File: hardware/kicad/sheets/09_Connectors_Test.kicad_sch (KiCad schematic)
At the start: 0 parts

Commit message: Complete ECO-003 hierarchy exposure
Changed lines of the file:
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@@
+    (effects (font (size 1.27 1.27)) (justify left))
+  )
+  (hierarchical_label "J6_I2C_SDA" (shape bidirectional) (at 100 60.24 0)
+    (effects (font (size 1.27 1.27)) (justify left))
+  )
+  (hierarchical_label "J6_I2C_SCL" (shape input) (at 100 65.32 0)
+    (effects (font (size 1.27 1.27)) (justify left))
+  )
+  (hierarchical_label "J7_I2C_SDA" (shape bidirectional) (at 100 70.40 0)
+    (effects (font (size 1.27 1.27)) (justify left))
+  )
+  (hierarchical_label "J7_I2C_SCL" (shape input) (at 100 75.48 0)
     (effects (font (size 1.27 1.27)) (justify left))
   )

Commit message: Implement Package 10R connector interfaces
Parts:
- added DFT1: T1 factory pogo logical boundary; not populated, symbol IPC100:CONN6
- added J1: P1/H01 controller input, symbol IPC100:CONN2
- added J10: D1/H10 ICD-001 optional DNP; no live mate, symbol IPC100:CONN4
- added J13: U1/H13 USB2 device-UFP grouped contacts, symbol IPC100:CONN12
- added J2: M1/H02 Axis 1 logic, symbol IPC100:CONN6
- added J3: M1/H03 Axis 2 logic, symbol IPC100:CONN6
- added J4: S1/H04 LEFT-RIGHT limits, symbol IPC100:CONN4
- added J5: S1/H05 UP-DOWN limits, symbol IPC100:CONN4
- added J6: D1/H06 OLED; 0.20m; no live mate, symbol IPC100:CONN5
- added J7: D1/H07 BME280; 0.20m; no live mate, symbol IPC100:CONN4
- added J8A: S1/H08A dedicated STOP; unique key, symbol IPC100:CONN2
- added J8B: L1/H08B ordinary UI; incompatible with J8A, symbol IPC100:CONN12
- added J9: R1/H09 SELV dry contact; 0-30VDC 1A, symbol IPC100:CONN3
- added R1: 5.1 kΩ ±1% CC1 Rd, symbol IPC100:R
- added R2: 5.1 kΩ ±1% CC2 Rd, symbol IPC100:R
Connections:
- net +3V3_CORE: now also DFT1.1, J8B.11
- net ARM_IN_RAW: now also J8B.6
- net AXIS1_LEN_SAFE: now also J2.1
- net AXIS1_LPWM_SAFE: now also J2.3
- net AXIS1_REN_SAFE: now also J2.2
- net AXIS1_RPWM_SAFE: now also J2.4
- net AXIS2_LEN_SAFE: now also J3.1
- net AXIS2_LPWM_SAFE: now also J3.3
- net AXIS2_REN_SAFE: now also J3.2
- net AXIS2_RPWM_SAFE: now also J3.4
- net BUZZER_OUT: now also J8B.1
- net ENCODER_A_RAW: now also J8B.9
- net ENCODER_B_RAW: now also J8B.8
- net ENCODER_SW_RAW: now also J8B.7
- net ESP_BOOT: now also DFT1.3
- net ESP_EN: now also DFT1.4
- net EXPANSION_VCC: now also J10.4
- net FIRE_IN_RAW: now also J8B.5
- net J10_I2C_SCL: now also J10.1
- net J10_I2C_SDA: now also J10.2
- net J6_I2C_SCL: now also J6.2
- net J6_I2C_SDA: now also J6.3
- net J7_I2C_SCL: now also J7.1
- net J7_I2C_SDA: now also J7.2
- net LIMIT_DOWN_RAW: now also J5.2
- net LIMIT_DOWN_RETURN: now also J5.1
- net LIMIT_LEFT_RAW: now also J4.4
- net LIMIT_LEFT_RETURN: now also J4.3
- net LIMIT_RIGHT_RAW: now also J4.2
- net LIMIT_RIGHT_RETURN: now also J4.1
- net LIMIT_UP_RAW: now also J5.4
- net LIMIT_UP_RETURN: now also J5.3
- net MOTOR_LOGIC_5V_A: now also J2.6
- net MOTOR_LOGIC_5V_B: now also J3.6
- net OLED_RESET: now also J6.1
- net OLED_VCC: now also J6.5
- net RELAY_COM: now also J9.2
- net RELAY_NC: now also J9.3
- net RELAY_NO: now also J9.1
- net RGB_B: now also J8B.2
- net RGB_G: now also J8B.3
- net RGB_R: now also J8B.4
- net SENSOR_VCC: now also J7.4
- net STOP_IN_RAW: now also J8A.2
- net STOP_RETURN: now also J8A.1
- net UART0_RX: now also DFT1.5
- net UART0_TX: now also DFT1.6
- net UI_VCC: now also J8B.10
- net USB_D+: now also J13.7, J13.8
- net USB_D-: now also J13.5, J13.6
- net USB_VBUS_RAW: now also J13.11, J13.12
- net VIN_RAW: now also J1.2
- new net GND: DFT1.2, J1.1, J10.3, J13.3, J13.4, J2.5, J3.5, J6.4, J7.3, J8B.12, R1.1, R2.1
- new net USB_CC1_RD_5K1: J13.10, R1.2
- new net USB_CC2_RD_5K1: J13.9, R2.2
- new net USB_SHIELD: J13.2
- no-connect marks 0 -> 1
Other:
- note added: "DFT1 FACTORY POGO: UART0_TX, UART0_RX, ESP_EN, ESP_BOOT, GND, +3V3_CORE sense-only; ground first; fixture never sources 3V3."
- note added: "J11 — DOCUMENTATION ONLY: spare GPIO concept; no symbol, pads, harness, or Rev A electrical connectivity. GPIO37 reserved."
- note added: "J12 — DOCUMENTATION ONLY: future CAN/RS485 concept; no symbol, pads, harness, or Rev A electrical connectivity."
- note added: "J13 U1: USB 2.0 DEVICE/UFP ONLY; 5.1k Rd on CC1/CC2 and connector ESD/shield options remain exact-part release items; no PD/host/source."
- note added: "PACKAGE 10R — ICD-002 PHYSICAL CONNECTOR BOUNDARIES; GENERIC SYMBOLS; NO FOOTPRINTS OR FINAL PART NUMBERS"

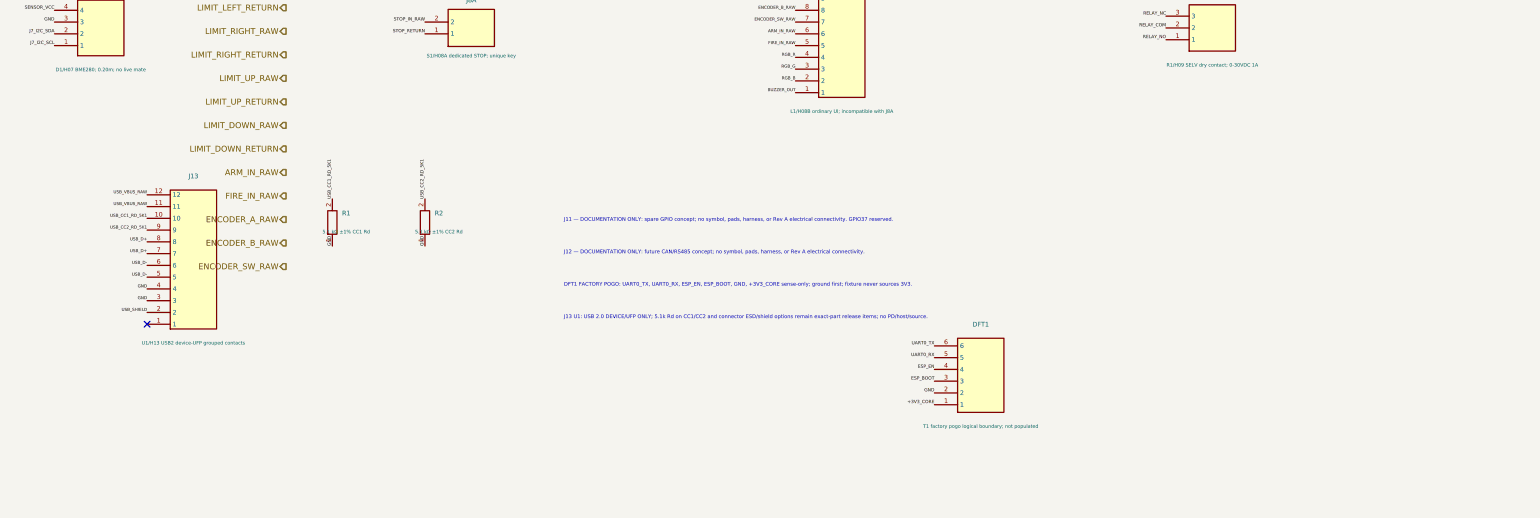
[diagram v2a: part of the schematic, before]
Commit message: Complete ECO-004 interface remediation
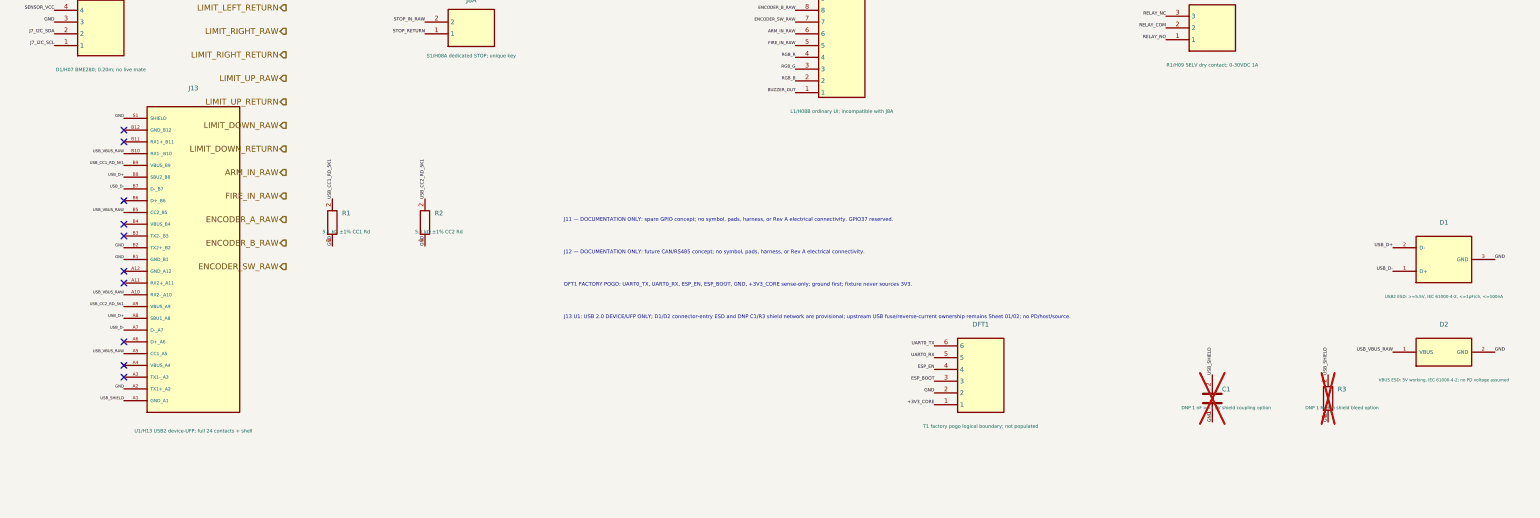
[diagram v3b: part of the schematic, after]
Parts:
- added C1: DNP 1 nF >=1 kV shield coupling option, symbol IPC100:C
- added D1: USB2 ESD: >=5.5V, IEC 61000-4-2, <=1pF/ch, <=100nA, symbol IPC100:USB_ESD2
- added D2: VBUS ESD: 5V working, IEC 61000-4-2; no PD voltag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, symbol IPC100:VBUS_ESD
- added R3: DNP 1 MOhm shield bleed option, symbol IPC100:R
- J13: value U1/H13 USB2 device-UFP grouped contacts -> U1/H13 USB2 device-UFP; full 24 contacts + shell; symbol IPC100:CONN12 -> IPC100:USB_C_UFP_FULL
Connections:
- net GND: now also J13.A2 (TX1+_A2), J13.B1 (GND_B1), J13.B2 (TX2+_B2), J13.S1 (SHIELD), C1.1, D1.3 (GND), D2.2 (GND), R3.1; no longer J13.3, J13.4
- net USB_CC1_RD_5K1: now also J13.B9 (VBUS_B9); no longer J13.10
- net USB_CC2_RD_5K1: now also J13.A9 (VBUS_A9); no longer J13.9
- net USB_D+: now also J13.A8 (SBU1_A8), J13.B8 (SBU2_B8), D1.2 (D-); no longer J13.7, J13.8
- net USB_D-: now also J13.A7 (D-_A7), J13.B7 (D-_B7), D1.1 (D+); no longer J13.5, J13.6
- net USB_SHIELD: now also J13.A1 (GND_A1), C1.2, R3.2; no longer J13.2
- net USB_VBUS_RAW: now also J13.A10 (RX2-_A10), J13.A5 (CC1_A5), J13.B10 (RX1-_B10), J13.B5 (CC2_B5), D2.1 (VBUS); no longer J13.11, J13.12
- no-connect marks 1 -> 10
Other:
- note added: "J13 U1: USB 2.0 DEVICE/UFP ONLY; D1/D2 connector-entry ESD and DNP C1/R3 shield network are provisional; upstream USB fuse/reverse-current ownership remains Sheet 01/02; no PD/host/source."
- note removed: "J13 U1: USB 2.0 DEVICE/UFP ONLY; 5.1k Rd on CC1/CC2 and connector ESD/shield options remain exact-part release items; no PD/host/source."

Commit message: Normalize Rev A reference designators
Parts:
- renumbered C1 to C901, D1 to D901, D2 to D902, R1 to R901, R2 to R902, R3 to R903
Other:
- note added: "J13 U1: USB 2.0 DEVICE/UFP ONLY; D901/D902 connector-entry ESD and DNP C901/R903 shield network are provisional; upstream USB fuse/reverse-current ownership remains Sheet 01/02; no PD/host/source."
- note removed: "J13 U1: USB 2.0 DEVICE/UFP ONLY; D1/D2 connector-entry ESD and DNP C1/R3 shield network are provisional; upstream USB fuse/reverse-current ownership remains Sheet 01/02; no PD/host/source."
